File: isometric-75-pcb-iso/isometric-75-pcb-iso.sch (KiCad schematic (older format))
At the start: 11 parts

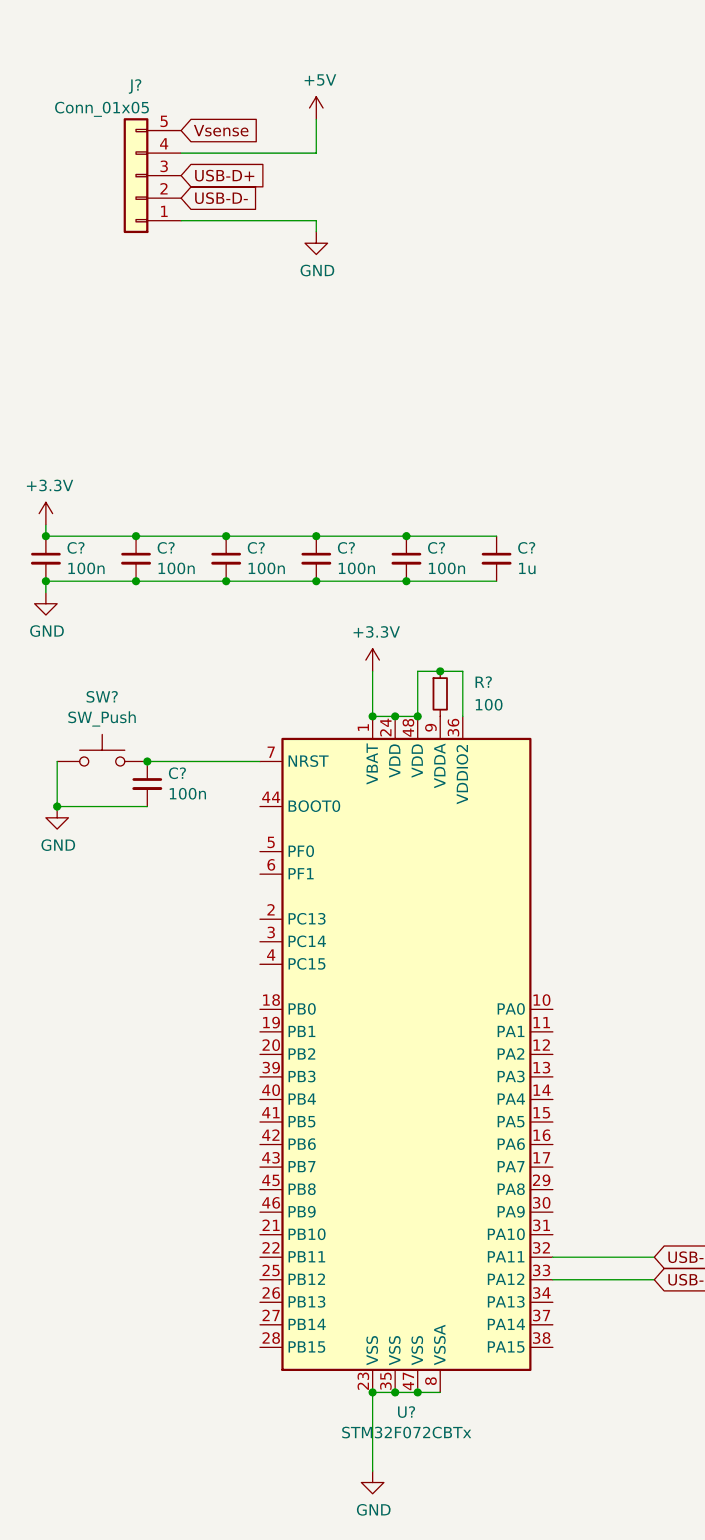
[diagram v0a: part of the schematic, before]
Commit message: assigned footprints
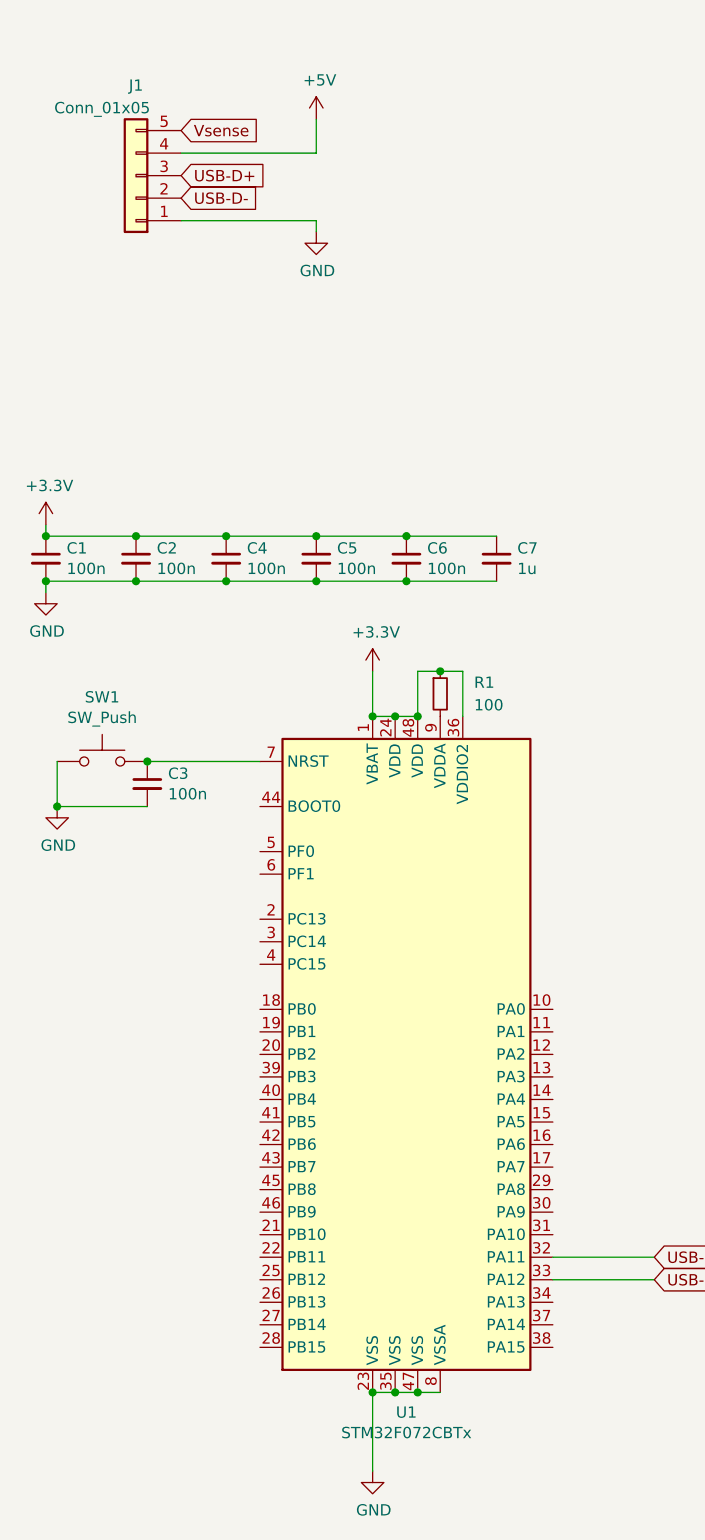
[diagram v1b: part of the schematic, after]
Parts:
- C1, C2, C3, C4, C5, C6, C7: renamed from C?; footprint (none) -> Capacitor_SMD:C_0402_1005Metric
- J1: renamed from J?; footprint Connector_JST:JST_PH_S5B-PH-SM4-TB_1x05-1MP_P2.00mm_Horizontal -> Connector_JST:JST_SH_SM05B-SRSS-TB_1x05-1MP_P1.00mm_Horizontal
- R1: renamed from R?; footprint (none) -> Resistor_SMD:R_0402_1005Metric
- SW1: renamed from SW?; footprint (none) -> random-keyboard-parts:SKQG-1155865
- gave numbers to parts that had none: 1
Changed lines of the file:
@@
 $EndDescr
 $Comp
-L MCU_ST_STM32F0:STM32F072CBTx U?
+L MCU_ST_STM32F0:STM32F072CBTx U1
 U 1 1 5E618B46
 P 2300 5150
-F 0 "U?" H 2250 3561 50  0000 C CNN
+F 0 "U1" H 2250 3561 50  0000 C CNN
 F 1 "STM32F072CBTx" H 2250 3470 50  0000 C CNN
 F 2 "Package_QFP:LQFP-48_7x7mm_P0.5mm" H 1700 3750 50  0001 R CNN
@@
 $EndComp
 $Comp
-L power:+3.3V #PWR?
+L power:+3.3V #PWR06
 U 1 1 5E620443
 P 2100 3450
-F 0 "#PWR?" H 2100 3300 50  0001 C CNN
+F 0 "#PWR06" H 2100 3300 50  0001 C CNN
 F 1 "+3.3V" H 2115 3623 50  0000 C CNN
 F 2 "" H 2100 3450 50  0001 C CNN
@@
 Connection ~ 2200 3650
 $Comp
-L power:GND #PWR?
+L power:GND #PWR07
 U 1 1 5E622DD3
 P 2100 7000
-F 0 "#PWR?" H 2100 6750 50  0001 C CNN
+F 0 "#PWR07" H 2100 6750 50  0001 C CNN
 F 1 "GND" H 2105 6827 50  0000 C CNN
 F 2 "" H 2100 7000 50  0001 C CNN
@@
 Connection ~ 2100 6650
 $Comp
-L Device:R_Small R?
+L Device:R_Small R1
 U 1 1 5E624452
 P 2400 3550
-F 0 "R?" H 2550 3600 50  0000 L CNN
+F 0 "R1" H 2550 3600 50  0000 L CNN
 F 1 "100" H 2550 3500 50  0000 L CNN
-F 2 "" H 2400 3550 50  0001 C CNN
+F 2 "Resistor_SMD:R_0402_1005Metric" H 2400 3550 50  0001 C CNN
 F 3 "~" H 2400 3550 50  0001 C CNN
 	1    2400 3550
@@
 Connection ~ 2400 3450
 $Comp
-L power:+3.3V #PWR?
+L power:+3.3V #PWR01
 U 1 1 5E625D2A
 P 650 2800
-F 0 "#PWR?" H 650 2650 50  0001 C CNN
+F 0 "#PWR01" H 650 2650 50  0001 C CNN
 F 1 "+3.3V" H 665 2973 50  0000 C CNN
 F 2 "" H 650 2800 50  0001 C CNN
@@
 $EndComp
 $Comp
-L power:GND #PWR?
+L power:GND #PWR02
 U 1 1 5E626CC8
 P 650 3100
-F 0 "#PWR?" H 650 2850 50  0001 C CNN
+F 0 "#PWR02" H 650 2850 50  0001 C CNN
 F 1 "GND" H 655 2927 50  0000 C CNN
 F 2 "" H 650 3100 50  0001 C CNN
@@
 $EndComp
 $Comp
-L Device:C_Small C?
+L Device:C_Small C1
 U 1 1 5E627ED9
 P 650 2950
-F 0 "C?" H 742 2996 50  0000 L CNN
+F 0 "C1" H 742 2996 50  0000 L CNN
 F 1 "100n" H 742 2905 50  0000 L CNN
-F 2 "" H 650 2950 50  0001 C CNN
+F 2 "Capacitor_SMD:C_0402_1005Metric" H 650 2950 50  0001 C CNN
 F 3 "~" H 650 2950 50  0001 C CNN
 	1    650  2950
@@
 $EndComp
 $Comp
-L Device:C_Small C?
+L Device:C_Small C2
 U 1 1 5E629144
 P 1050 2950
-F 0 "C?" H 1142 2996 50  0000 L CNN
+F 0 "C2" H 1142 2996 50  0000 L CNN
 F 1 "100n" H 1142 2905 50  0000 L CNN
-F 2 "" H 1050 2950 50  0001 C CNN
+F 2 "Capacitor_SMD:C_0402_1005Metric" H 1050 2950 50  0001 C CNN
 F 3 "~" H 1050 2950 50  0001 C CNN
 	1    1050 2950
@@
 $EndComp
 $Comp
-L Device:C_Small C?
+L Device:C_Small C4
 U 1 1 5E62A020
 P 1450 2950
-F 0 "C?" H 1542 2996 50  0000 L CNN
+F 0 "C4" H 1542 2996 50  0000 L CNN
 F 1 "100n" H 1542 2905 50  0000 L CNN
-F 2 "" H 1450 2950 50  0001 C CNN
+F 2 "Capacitor_SMD:C_0402_1005Metric" H 1450 2950 50  0001 C CNN
 F 3 "~" H 1450 2950 50  0001 C CNN
 	1    1450 2950
@@
 $EndComp
 $Comp
-L Device:C_Small C?
+L Device:C_Small C5
 U 1 1 5E62A663
 P 1850 2950
-F 0 "C?" H 1942 2996 50  0000 L CNN
+F 0 "C5" H 1942 2996 50  0000 L CNN
 F 1 "100n" H 1942 2905 50  0000 L CNN
-F 2 "" H 1850 2950 50  0001 C CNN
+F 2 "Capacitor_SMD:C_0402_1005Metric" H 1850 2950 50  0001 C CNN
 F 3 "~" H 1850 2950 50  0001 C CNN
 	1    1850 2950
@@
 $EndComp
 $Comp
-L Device:C_Small C?
+L Device:C_Small C6
 U 1 1 5E62AB00
 P 2250 2950
-F 0 "C?" H 2342 2996 50  0000 L CNN
+F 0 "C6" H 2342 2996 50  0000 L CNN
 F 1 "100n" H 2342 2905 50  0000 L CNN
-F 2 "" H 2250 2950 50  0001 C CNN
+F 2 "Capacitor_SMD:C_0402_1005Metric" H 2250 2950 50  0001 C CNN
 F 3 "~" H 2250 2950 50  0001 C CNN
 	1    2250 2950
@@
 $EndComp
 $Comp
-L Device:C_Small C?
+L Device:C_Small C7
 U 1 1 5E62B05E
 P 2650 2950
-F 0 "C?" H 2742 2996 50  0000 L CNN
+F 0 "C7" H 2742 2996 50  0000 L CNN
 F 1 "1u" H 2742 2905 50  0000 L CNN
-F 2 "" H 2650 2950 50  0001 C CNN
+F 2 "Capacitor_SMD:C_0402_1005Metric" H 2650 2950 50  0001 C CNN
 F 3 "~" H 2650 2950 50  0001 C CNN
 	1    2650 2950
@@
 	2900 6150 3350 6150
 $Comp
-L Switch:SW_Push SW?
+L Switch:SW_Push SW1
 U 1 1 5E6313B3
 P 900 3850
-F 0 "SW?" H 900 4135 50  0000 C CNN
+F 0 "SW1" H 900 4135 50  0000 C CNN
 F 1 "SW_Push" H 900 4044 50  0000 C CNN
-F 2 "" H 900 4050 50  0001 C CNN
+F 2 "random-keyboard-parts:SKQG-1155865" H 900 4050 50  0001 C CNN
 F 3 "~" H 900 4050 50  0001 C CNN
 	1    900  3850
@@
 $EndComp
 $Comp
-L power:GND #PWR?
+L power:GND #PWR03
 U 1 1 5E634A34
 P 700 4050
-F 0 "#PWR?" H 700 3800 50  0001 C CNN
+F 0 "#PWR03" H 700 3800 50  0001 C CNN
 F 1 "GND" H 705 3877 50  0000 C CNN
 F 2 "" H 700 4050 50  0001 C CNN
@@
 $EndComp
 $Comp
-L Device:C_Small C?
+L Device:C_Small C3
 U 1 1 5E638A0E
 P 1100 3950
-F 0 "C?" H 1192 3996 50  0000 L CNN
+F 0 "C3" H 1192 3996 50  0000 L CNN
 F 1 "100n" H 1192 3905 50  0000 L CNN
-F 2 "" H 1100 3950 50  0001 C CNN
+F 2 "Capacitor_SMD:C_0402_1005Metric" H 1100 3950 50  0001 C CNN
 F 3 "~" H 1100 3950 50  0001 C CNN
 	1    1100 3950
@@
 	1100 3850 1600 3850
 $Comp
-L Connector_Generic:Conn_01x05 J?
+L Connector_Generic:Conn_01x05 J1
 U 1 1 5E640E55
 P 1050 1250
-F 0 "J?" H 1050 850 50  0000 C CNN
+F 0 "J1" H 1050 850 50  0000 C CNN
 F 1 "Conn_01x05" H 1200 950 50  0000 C CNN
-F 2 "Connector_JST:JST_PH_S5B-PH-SM4-TB_1x05-1MP_P2.00mm_Horizontal" H 1050 1250 50  0001 C CNN
+F 2 "Connector_JST:JST_SH_SM05B-SRSS-TB_1x05-1MP_P1.00mm_Horizontal" H 1050 1250 50  0001 C CNN
 F 3 "http://www.jst-mfg.com/product/pdf/eng/ePH.pdf" H 1050 1250 50  0001 C CNN
 	1    1050 1250
@@
 $EndComp
 $Comp
-L power:GND #PWR?
+L power:GND #PWR05
 U 1 1 5E644973
 P 1850 1500
-F 0 "#PWR?" H 1850 1250 50  0001 C CNN
+F 0 "#PWR05" H 1850 1250 50  0001 C CNN
 F 1 "GND" H 1855 1327 50  0000 C CNN
 F 2 "" H 1850 1500 50  0001 C CNN
@@
 $EndComp
 $Comp
-L power:+5V #PWR?
+L power:+5V #PWR04
 U 1 1 5E645E1A
 P 1850 1000
-F 0 "#PWR?" H 1850 850 50  0001 C CNN
+F 0 "#PWR04" H 1850 850 50  0001 C CNN
 F 1 "+5V" H 1865 1173 50  0000 C CNN
 F 2 "" H 1850 1000 50  0001 C CNN

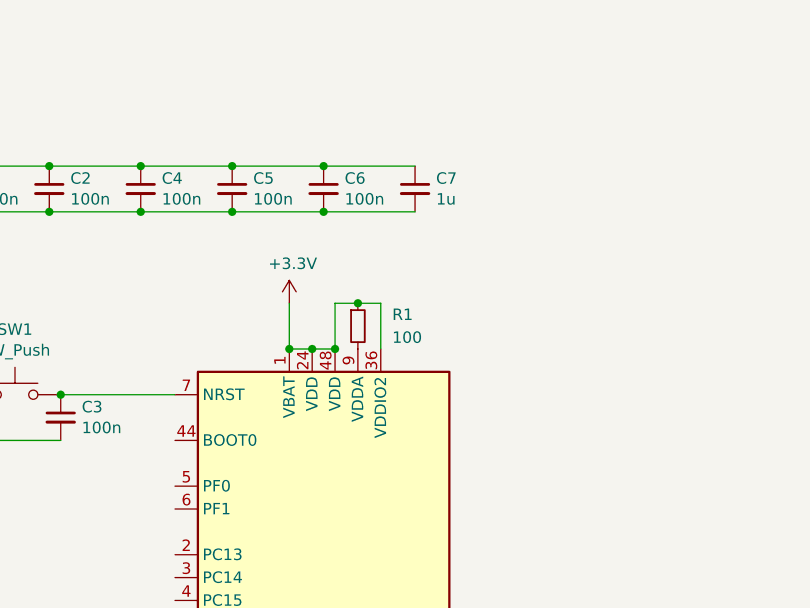
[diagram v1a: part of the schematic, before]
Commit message: wired switches and leds
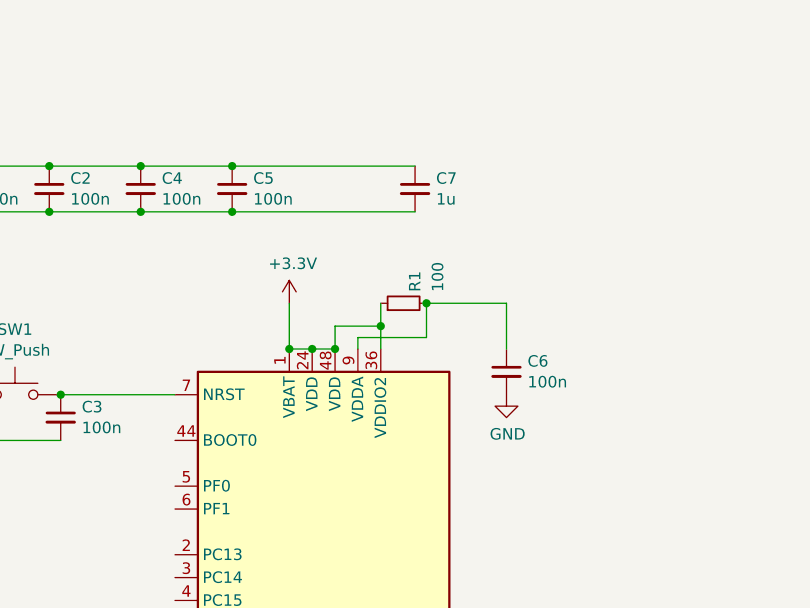
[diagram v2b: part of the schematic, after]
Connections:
- net +3V3: no longer C6.1
- net at R1.2, U1.9 (VDDA): now also C6.1
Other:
- moved on the sheet: C6, R1
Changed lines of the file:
@@
 Connection ~ 2100 6650
-$Comp
-L Device:R_Small R1
-U 1 1 5E624452
-P 2400 3550
-F 0 "R1" H 2550 3600 50  0000 L CNN
-F 1 "100" H 2550 3500 50  0000 L CNN
-F 2 "Resistor_SMD:R_0402_1005Metric" H 2400 3550 50  0001 C CNN
-F 3 "~" H 2400 3550 50  0001 C CNN
-	1    2400 3550
-	1    0    0    -1
-$EndComp
-Wire Wire Line
-	2500 3650 2500 3450
-Wire Wire Line
-	2500 3450 2400 3450
-Wire Wire Line
-	2300 3450 2300 3650
-Connection ~ 2300 3650
-Wire Wire Line
-	2300 3450 2400 3450
-Connection ~ 2400 3450
 $Comp
 L power:+3.3V #PWR01
@@
 L Device:C_Small C6
 U 1 1 5E62AB00
-P 2250 2950
-F 0 "C6" H 2342 2996 50  0000 L CNN
-F 1 "100n" H 2342 2905 50  0000 L CNN
-F 2 "Capacitor_SMD:C_0402_1005Metric" H 2250 2950 50  0001 C CNN
-F 3 "~" H 2250 2950 50  0001 C CNN
-	1    2250 2950
+P 3050 3750
+F 0 "C6" H 3142 3796 50  0000 L CNN
+F 1 "100n" H 3142 3705 50  0000 L CNN
+F 2 "Capacitor_SMD:C_0402_1005Metric" H 3050 3750 50  0001 C CNN
+F 3 "~" H 3050 3750 50  0001 C CNN
+	1    3050 3750
 	1    0    0    -1
 $EndComp
@@
 	1450 2850 1850 2850
 Connection ~ 1450 2850
-Wire Wire Line
-	1850 2850 2250 2850
 Connection ~ 1850 2850
-Wire Wire Line
-	2250 2850 2650 2850
-Connection ~ 2250 2850
-Wire Wire Line
-	2650 3050 2250 3050
-Wire Wire Line
-	2250 3050 1850 3050
-Connection ~ 2250 3050
 Wire Wire Line
 	1850 3050 1450 3050
@@
 F1 "matrix.sch" 50
 $EndSheet
+Wire Wire Line
+	1850 3050 2650 3050
+Wire Wire Line
+	1850 2850 2650 2850
+Wire Wire Line
+	2500 3550 2300 3550
+Wire Wire Line
+	2300 3550 2300 3650
+Wire Wire Line
+	2500 3550 2500 3650
+Connection ~ 2300 3650
+Wire Wire Line
+	3050 3450 3050 3650
+$Comp
+L power:GND #PWR0101
+U 1 1 5EFE1B26
+P 3050 3850
+F 0 "#PWR0101" H 3050 3600 50  0001 C CNN
+F 1 "GND" H 3055 3677 50  0000 C CNN
+F 2 "" H 3050 3850 50  0001 C CNN
+F 3 "" H 3050 3850 50  0001 C CNN
+	1    3050 3850
+	1    0    0    -1
+$EndComp
+$Comp
+L Device:R_Small R1
+U 1 1 5E624452
+P 2600 3450
+F 0 "R1" H 2650 3400 50  0000 L CNN
+F 1 "100" H 2650 3300 50  0000 L CNN
+F 2 "Resistor_SMD:R_0402_1005Metric" H 2600 3450 50  0001 C CNN
+F 3 "~" H 2600 3450 50  0001 C CNN
+	1    2600 3450
+	0    -1   -1   0
+$EndComp
+Wire Wire Line
+	2500 3450 2500 3550
+Connection ~ 2500 3550
+Wire Wire Line
+	2700 3450 2700 3600
+Wire Wire Line
+	2700 3600 2400 3600
+Wire Wire Line
+	2400 3600 2400 3650
+Wire Wire Line
+	3050 3450 2700 3450
+Connection ~ 2700 3450
 $EndSCHEMATC

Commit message: continued the pcb
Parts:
- added C101, C103: 1u, Capacitor_SMD:C_0402_1005Metric, symbol Device:C_Small
- added C110: 100n, Capacitor_SMD:C_0402_1005Metric, symbol Device:C_Small
- added J102: Conn_01x06, Connector_JST:JST_SH_SM06B-SRSS-TB_1x06-1MP_P1.00mm_Horizontal, symbol Connector_Generic:Conn_01x06
- added Q101: AO3400A, Package_TO_SOT_SMD:SOT-23, symbol Device:Q_NMOS_GSD
- added R102, R103: 10k, Resistor_SMD:R_0402_1005Metric, symbol Device:R_Small
- added R104: 100, Resistor_SMD:R_0402_1005Metric, symbol Device:R_Small
- added U101: XC6206P332MR, Package_TO_SOT_SMD:SOT-23, symbol Regulator_Linear:XC6206PxxxMR
- renumbered C3 to C102, C1 to C104, C2 to C105, C6 to C106, C4 to C107, C5 to C108, C7 to C109, J1 to J101, R1 to R101, SW1 to SW101, U1 to U102
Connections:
- net +3V3: now also C103.1, U101.2 (VO)
- net +5V: now also C101.1, J102.6 (Pin_6), U101.3 (VI)
- net GND: now also C101.2, C103.2, C110.2, J102.1 (Pin_1), Q101.2 (S), R103.2, U101.1 (GND)
- net Vsense: now also R102.1
- net SPI_NSS: now reaches U102.14 (PA4)
- net SPI_NSS: now also J102.2 (Pin_2)
- net SPI_SCK: now reaches U102.15 (PA5)
- net SPI_SCK: now also J102.3 (Pin_3)
- net SPI_MISO: now reaches U102.16 (PA6)
- net SPI_MISO: now also J102.4 (Pin_4)
- net SPI_MOSI: now reaches U102.17 (PA7)
- net SPI_MOSI: now also J102.5 (Pin_5)
- net at U102.19 (PB1): now also C110.1, R102.2, R103.1
- net LED_PWM: now reaches U102.34 (PA13)
- net LED_PWM: now also R104.1
- new net: Q101.1 (G), R104.2
- new net LED-: Q101.3 (D)
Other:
- moved on the sheet: C104, C105, C107, C108, C109
